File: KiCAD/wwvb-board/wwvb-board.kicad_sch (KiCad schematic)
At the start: 1 part, among them J1 Conn_01x07

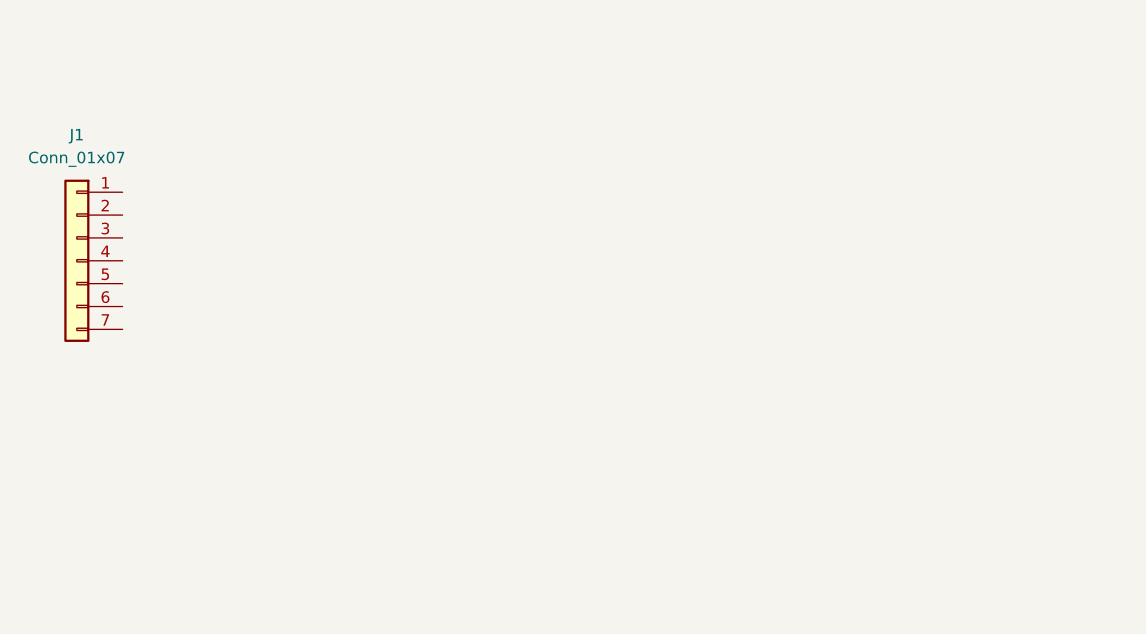
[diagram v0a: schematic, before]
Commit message: start possible WWVB board, update README
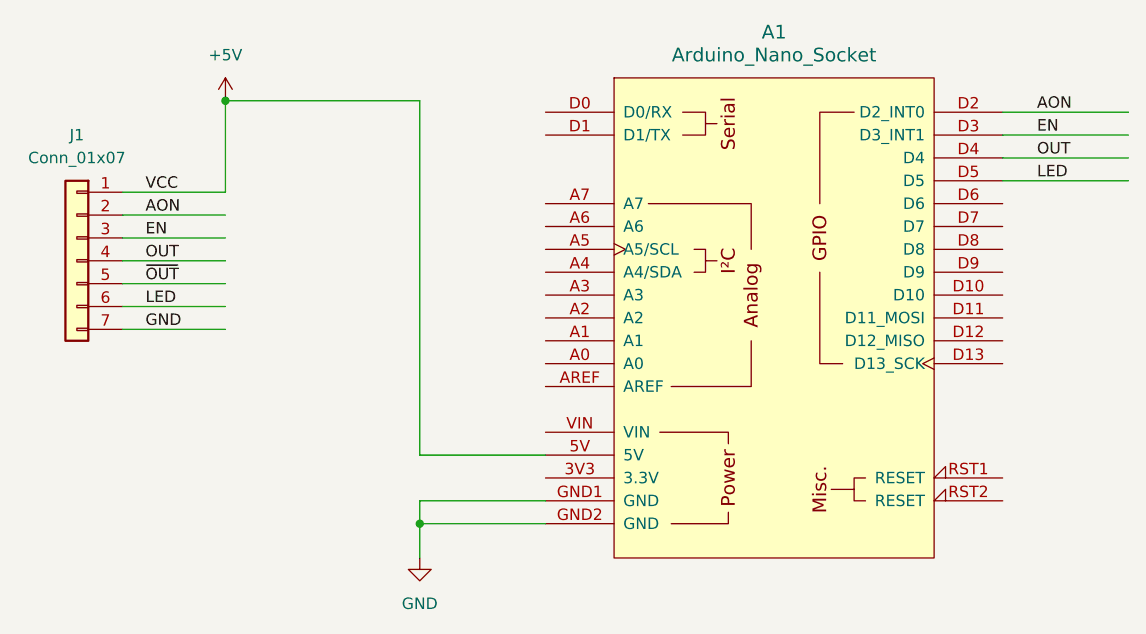
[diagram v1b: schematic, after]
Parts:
- added A1: Arduino_Nano_Socket, PCM_arduino-library:Arduino_Nano_Socket, symbol arduino-library:Arduino_Nano_Socket
- J1: footprint (none) -> my_WWV:Canaduino_V4
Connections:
- net +5V: now reaches J1.1 (Pin_1)
- net +5V: now also A1.5V
- net AON: now reaches J1.2 (Pin_2)
- net AON: now also A1.D2 (D2_INT0)
- net EN: now reaches J1.3 (Pin_3)
- net EN: now also A1.D3 (D3_INT1)
- net OUT: now reaches J1.4 (Pin_4)
- net OUT: now also A1.D4
- net ~{OUT}: now reaches J1.5 (Pin_5)
- net LED: now reaches J1.6 (Pin_6)
- net LED: now also A1.D5
- net GND: now reaches J1.7 (Pin_7)
- net GND: now also A1.GND1 (GND), A1.GND2 (GND)
